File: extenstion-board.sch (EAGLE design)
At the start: 13 parts

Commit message: added provision screw plug
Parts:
- removed X1, X10, X11, X12, X13, X2, X3, X4, X5, X6, X7, X8, X9: (no value), con-wago-500:W237-102
- added J1, J10, J11, J12, J13, J2, J3, J4, J5, J6, J7, J8, J9: (no value), SparkFun-Connectors:CONN_02PTH4
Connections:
- net +12V: now also J1.1, J10.2, J2.2, J4.1, J5.2, J7.1, J8.2; no longer X1-2.KL, X13-1.KL, X2-1.KL, X4-2.KL, X5-1.KL, X7-2.KL, X8-1.KL
- net GND: now also J1.2, J10.1, J3.1, J4.2, J6.1, J7.2, J9.1; no longer X1-1.KL, X13-2.KL, X3-2.KL, X4-1.KL, X6-2.KL, X7-1.KL, X9-2.KL
- net N$1: now also J11.2, J8.1; no longer X12-1.KL, X8-2.KL
- net N$2: now also J13.2, J2.1; no longer X10-1.KL, X2-2.KL
- net N$3: now also J13.1, J3.2; no longer X10-2.KL, X3-1.KL
- net N$4: now also J12.2, J5.1; no longer X11-1.KL, X5-2.KL
- net N$5: now also J12.1, J6.2; no longer X11-2.KL, X6-1.KL
- net N$6: now also J11.1, J9.2; no longer X12-2.KL, X9-1.KL

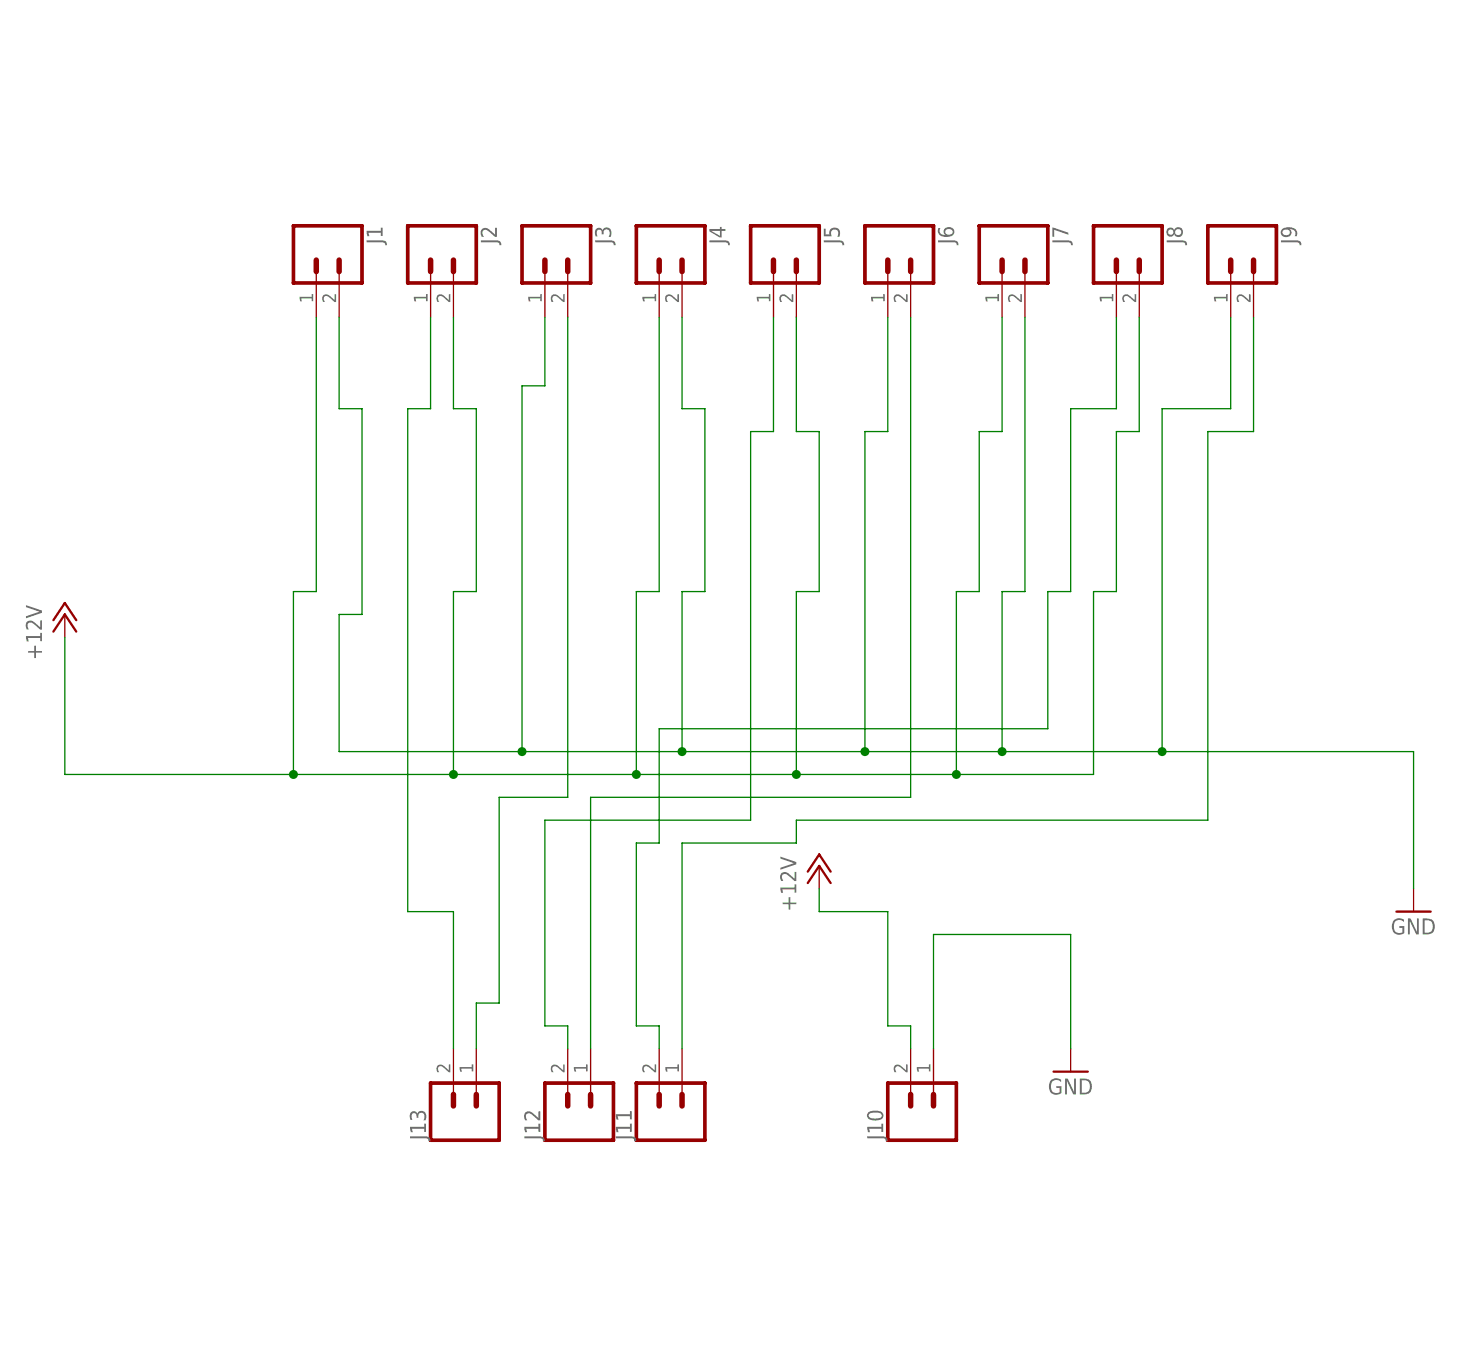
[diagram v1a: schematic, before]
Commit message: added holes for pillers
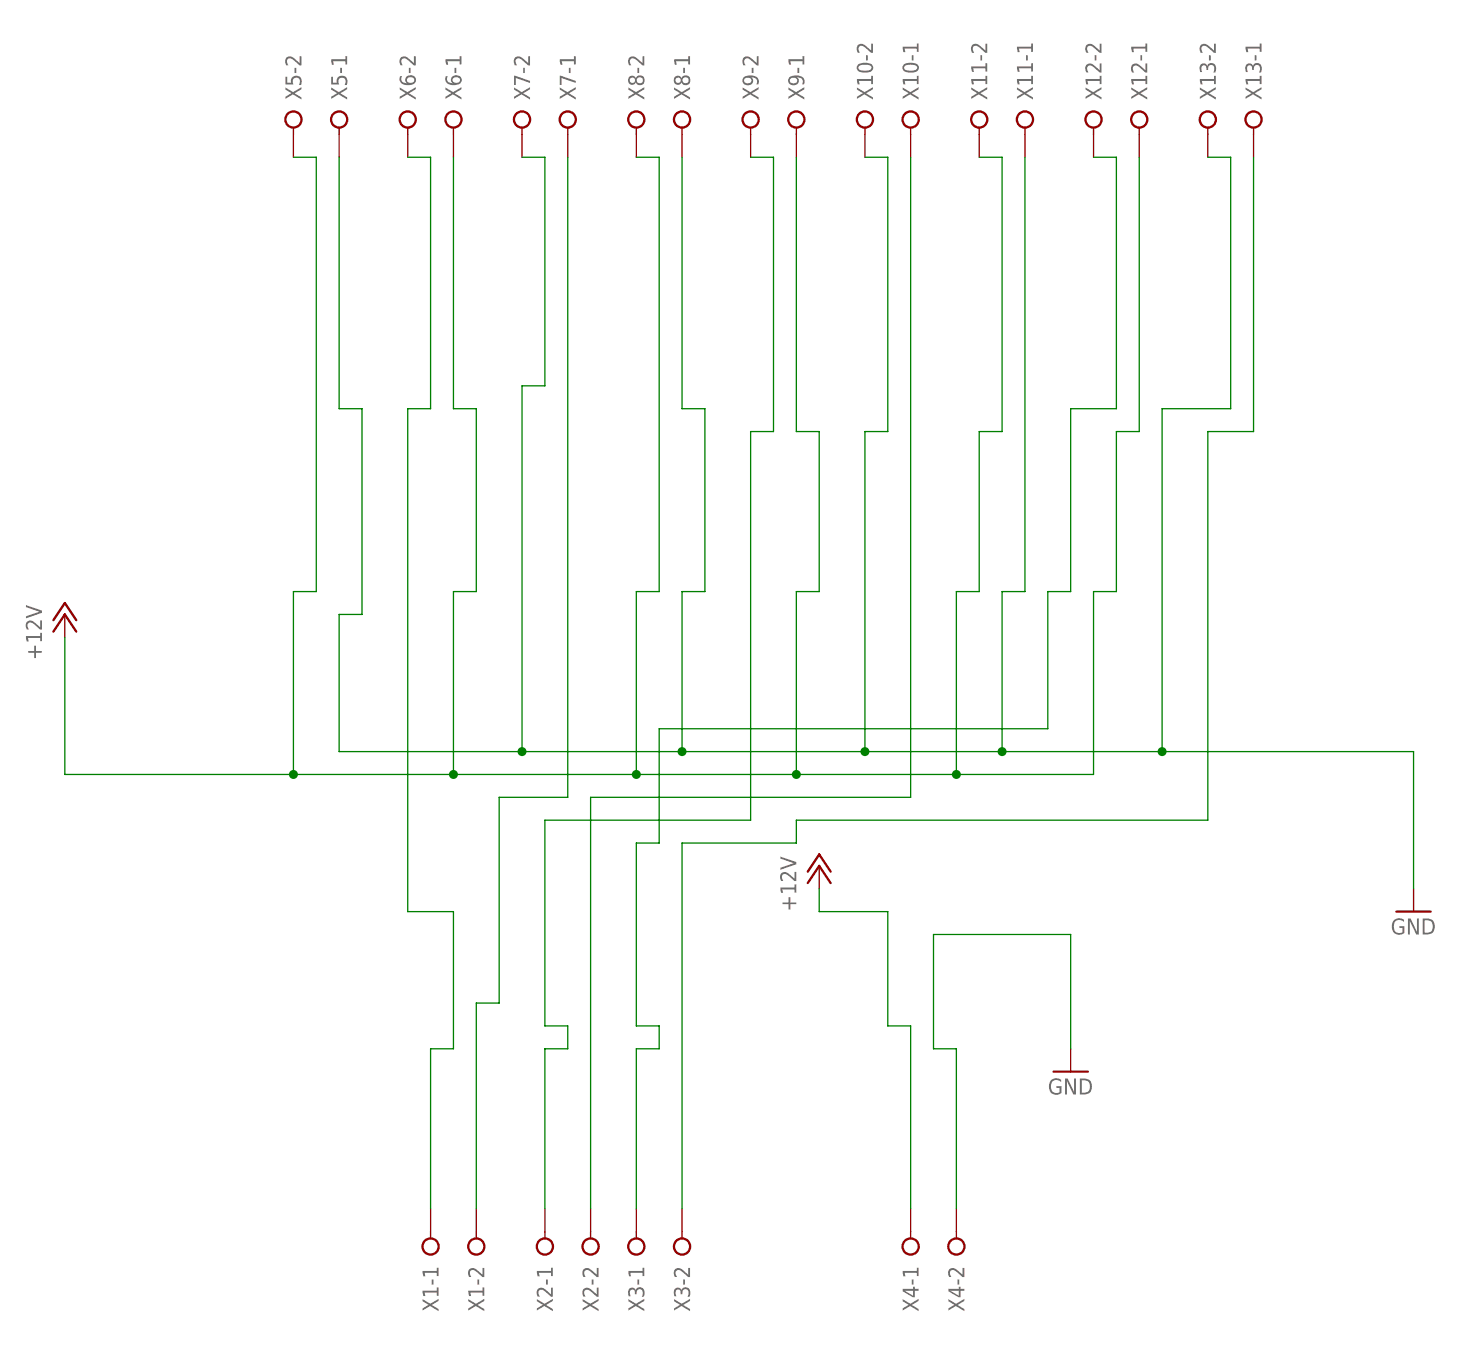
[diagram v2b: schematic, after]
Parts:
- removed J1, J10, J11, J12, J13, J2, J3, J4, J5, J6, J7, J8, J9: (no value), SparkFun-Connectors:CONN_02PTH4
- added X1, X10, X11, X12, X13, X2, X3, X4, X5, X6, X7, X8, X9: (no value), pluggable-con:W237-02P
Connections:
- net +12V: now also X11-2.KL, X12-1.KL, X4-1.KL, X5-2.KL, X6-1.KL, X8-2.KL, X9-1.KL; no longer J1.1, J10.2, J2.2, J4.1, J5.2, J7.1, J8.2
- net GND: now also X10-2.KL, X11-1.KL, X13-2.KL, X4-2.KL, X5-1.KL, X7-2.KL, X8-1.KL; no longer J1.2, J10.1, J3.1, J4.2, J6.1, J7.2, J9.1
- net N$1: now also X12-2.KL, X3-1.KL; no longer J11.2, J8.1
- net N$2: now also X1-1.KL, X6-2.KL; no longer J13.2, J2.1
- net N$3: now also X1-2.KL, X7-1.KL; no longer J13.1, J3.2
- net N$4: now also X2-1.KL, X9-2.KL; no longer J12.2, J5.1
- net N$5: now also X10-1.KL, X2-2.KL; no longer J12.1, J6.2
- net N$6: now also X13-1.KL, X3-2.KL; no longer J11.1, J9.2
